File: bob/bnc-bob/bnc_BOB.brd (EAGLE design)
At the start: 35.6 x 96.8 mm, 9 parts

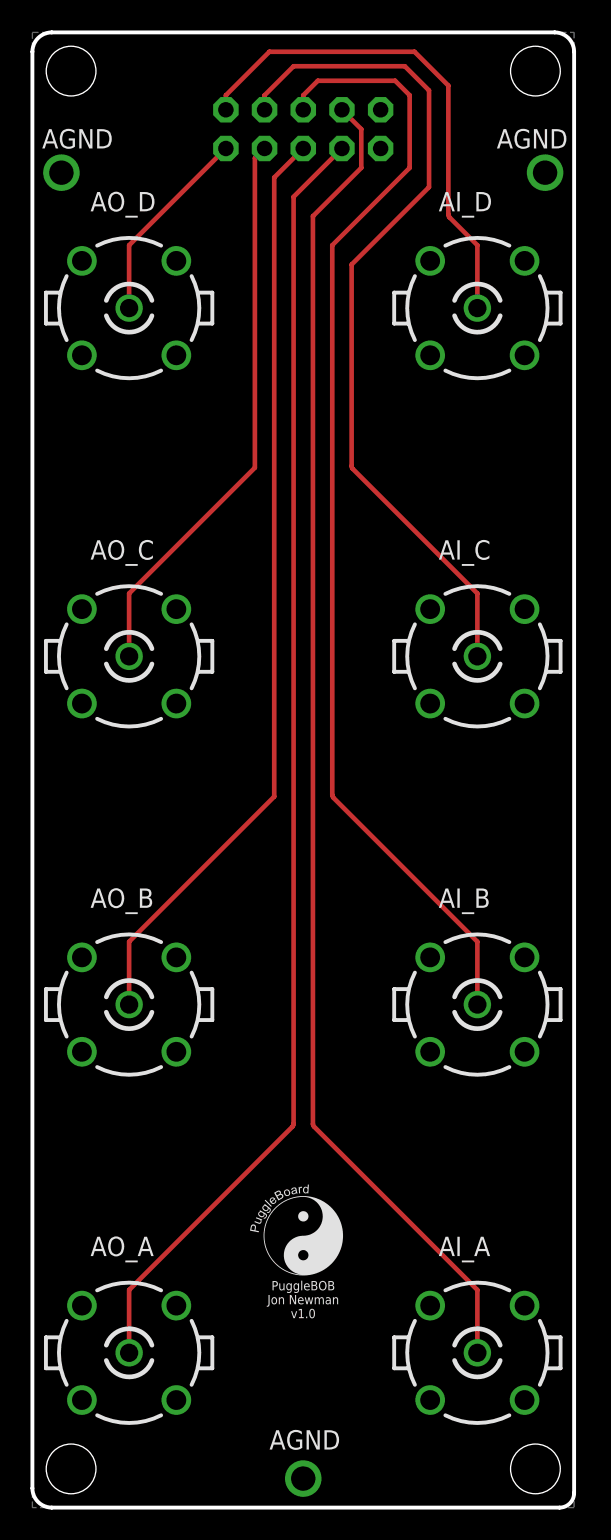
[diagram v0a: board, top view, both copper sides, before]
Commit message: Added back missing board file.
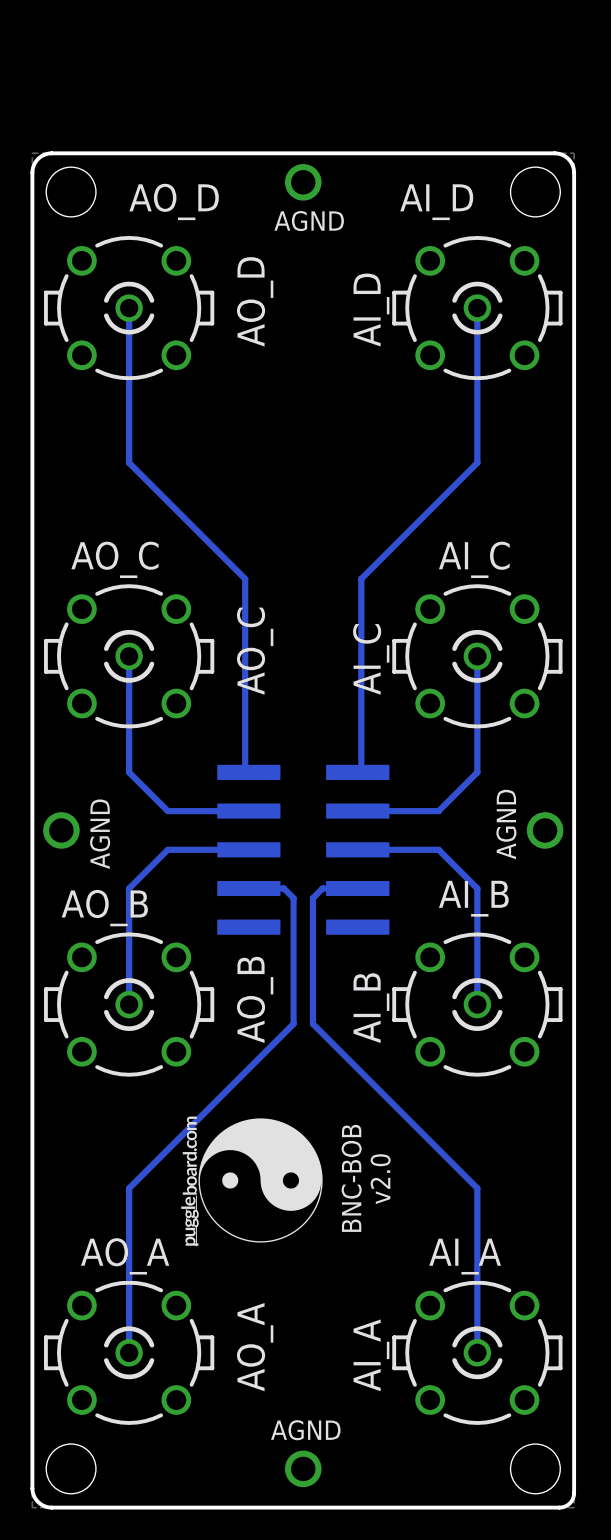
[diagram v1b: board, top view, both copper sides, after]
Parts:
- added U$1: (no value), puggleboard:PB-LOGO
- added U$2: (no value), ohw-logo:OSHW_FILLX500_NOTEXT
- AI_B, AI_C, AI_D, AO_A, AO_B, AO_C, AO_D: device con-coax:B35N61 -> puggleboard:B35N61
- A_I/O: value PINHD-2X5 -> PINHD-2X5-IDC-SMD; device adafruit:2X05 -> puggleboard:2X05-IDC-SMD
- moved A_I/O 47.3 mm to (17.8, 43.2), turned to 180 degrees
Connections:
- net ADC_A: now also A_I/O.P$4; no longer A_I/O.4
- net ADC_B: now also A_I/O.P$6; no longer A_I/O.6
- net ADC_C: now also A_I/O.P$8; no longer A_I/O.8
- net ADC_D: now also A_I/O.P$10; no longer A_I/O.10
- net AGND: now also A_I/O.P$1, A_I/O.P$2; no longer A_I/O.1, A_I/O.2
- net DAC_A: now also A_I/O.P$3; no longer A_I/O.3
- net DAC_B: now also A_I/O.P$5; no longer A_I/O.5
- net DAC_C: now also A_I/O.P$7; no longer A_I/O.7
- net DAC_D: now also A_I/O.P$9; no longer A_I/O.9
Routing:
- net ADC_B: track 74.5 -> 16.5 mm
- net ADC_A: track 87.9 -> 37.5 mm
- net DAC_A: track 84.8 -> 37.5 mm
- net DAC_B: track 60.9 -> 16.5 mm
- net ADC_C: track 55.8 -> 16.5 mm
- net DAC_D: track 13.1 -> 33.7 mm
- net DAC_C: track 37.0 -> 16.5 mm
- net ADC_D: track 33.0 -> 33.7 mm
- added copper zone on layer 1, net AGND
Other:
- board size 35.6 x 96.8 mm -> 35.6 x 88.9 mm
- board text added: "AI_A"
- board text added: "AI_B"
- board text added: "AI_C"
- board text added: "AI_D"
- board text added: "AO_A"
- board text added: "AO_B"
- board text added: "AO_C"
- board text added: "AO_D"
- board text added: "BNC-BOB v2.0"
- board text added: "S/N:"
- board text removed: "PuggleBOB Jon Newman v1.0"

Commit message: Finished BOMs (and integrated parts into database) for all the BOBs. Now must do for the main board. Will take a while.
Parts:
- AI_A: device con-coax:B35N61 -> puggleboard:B35N61
